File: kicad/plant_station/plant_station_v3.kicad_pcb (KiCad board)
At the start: 2 copper layers, 73.4 x 43 mm, 89 parts, among them IC1 VEML7700-TT, IC3 TLC555CDR, IC4 ADC081C021CIMK_NOPB, J1 Conn_02x08_Odd_Even, J10 I2C HOST, J11 SOIL_I2C, J12 WEATHER_I2C, J13 ZF5S-20-01-T-WT-TR, J14 505567-0471, J15 505567-0471, J16 Conn_01x06, J17 Conn_01x08, J18 Conn_01x08, J19 Ammeter_Jumper, J2 MB_I2C, J3 MB_I2C, J4 ZF5S-20-01-T-WT-TR, J5 MB_I2C, J6 MB_I2C, J7 Conn_01x08, J8 Conn_01x06, J9 I2C SCREEN, P1 USB_C_Plug_USB2.0, Q1 DTC113Z, Q3 DTC113Z, Q4 DMG2301L, Q5 BC817DS,115, U1 HDC2010YPAT, U4 ESP-WROOM-02, U5 TPL5110, U6 CP2102N-A01-GQFN28

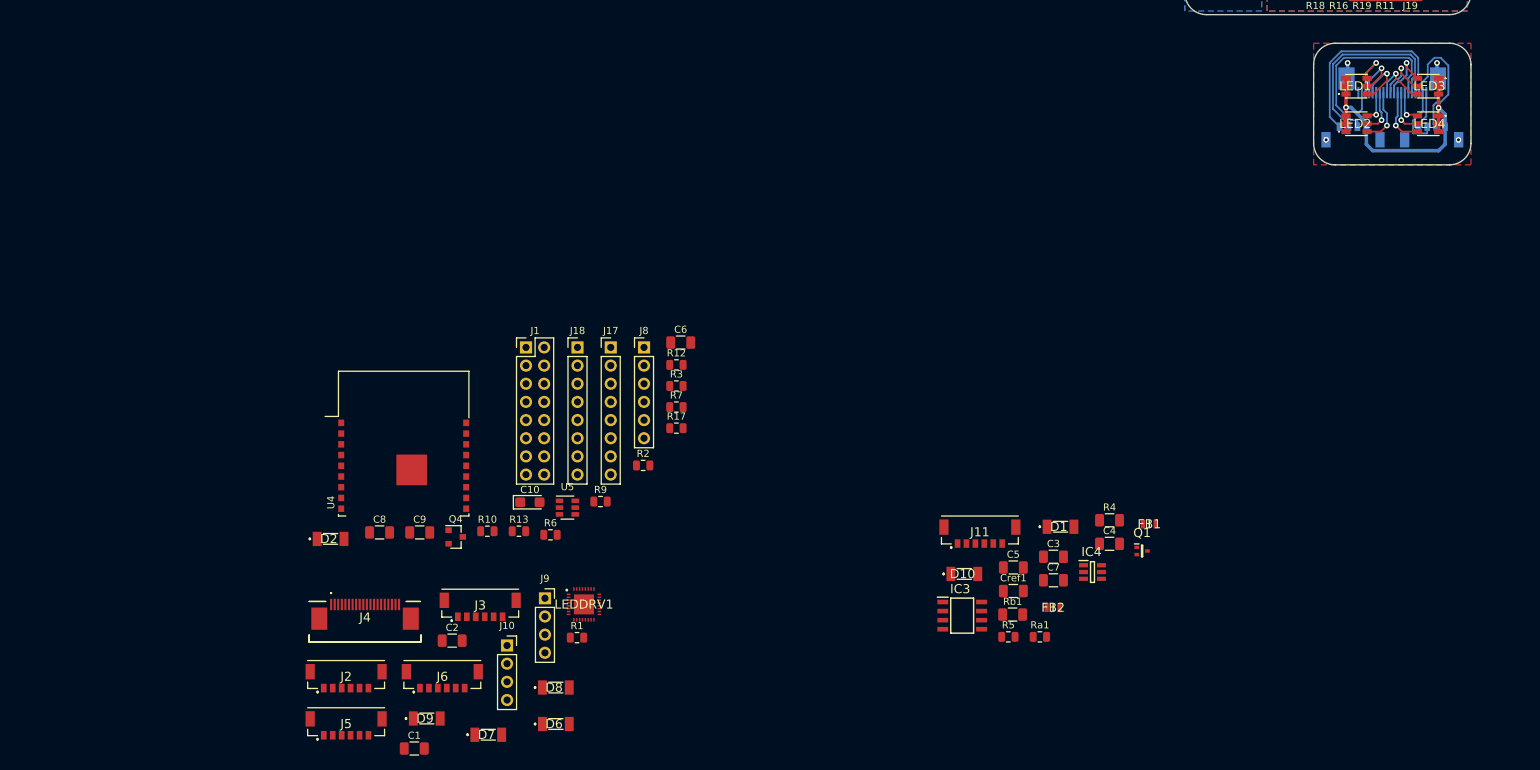
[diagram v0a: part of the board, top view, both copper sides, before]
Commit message: Moved the LED driver to LEDs board, refactored connectors. Hopefuly PCBNEW could update it all in place
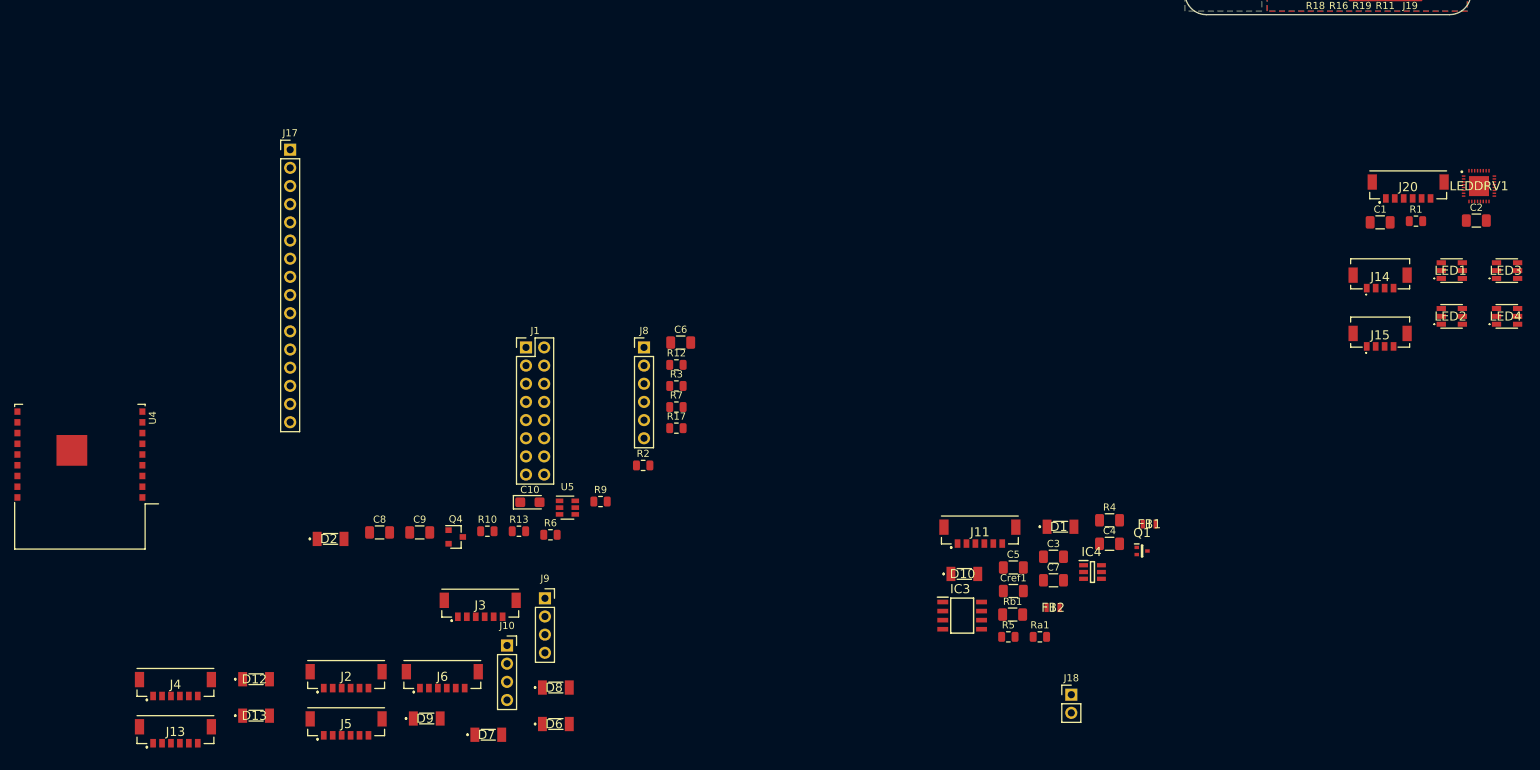
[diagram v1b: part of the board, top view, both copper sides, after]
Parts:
- added D12: LS4148, Parts:MELF_SOD_80_3_BZT55B13GS08, F.Cu at (84.1, 129.9)
- added D13: LS4148, Parts:MELF_SOD_80_3_BZT55B13GS08, F.Cu at (84.1, 135.0)
- added J20: LED_I2C, Parts:Molex_Conn_SMD_01x06_505567_0671, F.Cu at (245.2, 61.1)
- J13: value ZF5S-20-01-T-WT-TR -> MB_I2C; footprint Parts:ZF5S2001TWTTR -> Parts:Molex_Conn_SMD_01x06_505567_0671; moved to F.Cu
- J14: value 505567-0471 -> Ambient_Led_6; moved to F.Cu
- J15: value 505567-0471 -> Ambient_Led_5; moved to F.Cu
- J17: value Conn_01x08 -> GPIO; footprint Connector_PinHeader_2.54mm:PinHeader_1x08_P2.54mm_Vertical -> Connector_PinHeader_2.54mm:PinHeader_1x16_P2.54mm_Vertical
- J18: value Conn_01x08 -> ALWAYS_ON; footprint Connector_PinHeader_2.54mm:PinHeader_1x08_P2.54mm_Vertical -> Connector_PinHeader_2.54mm:PinHeader_1x02_P2.54mm_Vertical
- J4: value ZF5S-20-01-T-WT-TR -> MB_I2C; footprint Parts:ZF5S2001TWTTR -> Parts:Molex_Conn_SMD_01x06_505567_0671
- J8: value Conn_01x06 -> UART
- moved J13 193.3 mm to (72.9, 137.3)
- moved C2 154.8 mm to (254.8, 65.8)
- moved C1 153.8 mm to (241.3, 66.0)
- moved LEDDRV1 138.1 mm to (255.1, 61.0)
- moved R1 131.0 mm to (246.3, 65.9)
- moved J18 84.4 mm to (198.1, 132.1)
- moved J17 52.7 mm to (88.9, 55.9)
- moved U4 45.3 mm to (59.5, 98.5), turned to 180 degrees
- moved LED2 30.1 mm to (251.3, 79.2)
- moved LED4 29.1 mm to (259.0, 79.2), turned to 0 degrees
- moved LED1 29.0 mm to (251.3, 72.8)
- moved LED3 28.1 mm to (259.0, 72.8), turned to 0 degrees
- moved J4 27.9 mm to (72.9, 130.7)
- moved J15 27.8 mm to (241.3, 81.8)
- moved J14 20.7 mm to (241.3, 73.7)
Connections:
- net /env_sensor/HOST_WAKE renamed Net-(J12-Pad5)
- D2 pad 2: /HOST_WAKE -> /esp8266/WAKE_UP
- J1 pad 5: Net-(J1-Pad5) -> /esp8266/GPIO16
- J1 pad 6: Net-(J1-Pad6) -> /esp8266/WAKE_UP
- J1 pad 7: Net-(J1-Pad11) -> Net-(J1-Pad7)
- J13 pad 3: /leds/LED_1_R -> /SDA
- J13 pad 4: /leds/LED_1_G -> /SCL
- J13 pad 5: /leds/LED_1_B -> /HOST_WAKE
- J13 pad 6: /leds/LED_2_R -> Net-(D13-Pad1)
- J14 pad 5: Net-(J13-PadMP1) -> Net-(J14-Pad5)
- J14 pad 6: Net-(J13-PadMP1) -> Net-(J14-Pad5)
- J15 pad 5: Net-(J13-PadMP1) -> Net-(J14-Pad5)
- J15 pad 6: Net-(J13-PadMP1) -> Net-(J14-Pad5)
- J17 pad 3: /esp8266/ESP_RST -> /SDA
- J17 pad 4: /esp8266/ESP_EN -> /SCL
- J17 pad 5: /HOST_WAKE -> /esp8266/WAKE_UP
- J17 pad 6: /SDA -> /ALL_EN
- J17 pad 7: /SCL -> /esp8266/ESP_RST
- J17 pad 8: Net-(J17-Pad8) -> /esp8266/ESP_EN
- J18 pad 1: GND -> Net-(FB2-Pad1)
- J18 pad 2: +3V3 -> GND
- J2 pad MP1: Net-(J2-PadMP1) -> Net-(J13-PadMP1)
- J2 pad MP2: Net-(J2-PadMP2) -> Net-(J13-PadMP1)
- J3 pad MP1: Net-(J3-PadMP1) -> Net-(J13-PadMP1)
- J3 pad MP2: Net-(J3-PadMP2) -> Net-(J13-PadMP1)
- J4 pad 3: /LED_1_R -> /SDA
- J4 pad 4: /LED_1_G -> /SCL
- J4 pad 5: /LED_1_B -> /HOST_WAKE
- J4 pad 6: /LED_2_R -> Net-(D12-Pad1)
- J4 pad MP1: GND -> Net-(J13-PadMP1)
- J4 pad MP2: GND -> Net-(J13-PadMP1)
- J5 pad MP1: Net-(J5-PadMP1) -> Net-(J13-PadMP1)
- J5 pad MP2: Net-(J5-PadMP2) -> Net-(J13-PadMP1)
- J6 pad MP1: Net-(J6-PadMP1) -> Net-(J13-PadMP1)
- J6 pad MP2: Net-(J6-PadMP2) -> Net-(J13-PadMP1)
- LEDDRV1 pad 1: /LED_1_R -> /leds/LED_1_R
- LEDDRV1 pad 10: /LED_4_R -> /leds/LED_4_R
- LEDDRV1 pad 11: /LED_4_G -> /leds/LED_4_G
- LEDDRV1 pad 12: /LED_4_B -> /leds/LED_4_B
- LEDDRV1 pad 13: /LED_5_R -> /leds/LED_5_R
- LEDDRV1 pad 14: /LED_5_G -> /leds/LED_5_G
- LEDDRV1 pad 15: /LED_5_B -> /leds/LED_5_B
- LEDDRV1 pad 16: /LED_6_R -> /leds/LED_6_R
- LEDDRV1 pad 17: /LED_6_G -> /leds/LED_6_G
- LEDDRV1 pad 18: /LED_6_B -> /leds/LED_6_B
- LEDDRV1 pad 2: /LED_1_G -> /leds/LED_1_G
- LEDDRV1 pad 28: /SDA -> /leds/SDA
- LEDDRV1 pad 29: /SCL -> /leds/SCL
- LEDDRV1 pad 3: /LED_1_B -> /leds/LED_1_B
- LEDDRV1 pad 30: /ALL_EN -> /leds/ALL_EN
- LEDDRV1 pad 4: /LED_2_R -> /leds/LED_2_R
- LEDDRV1 pad 5: /LED_2_G -> /leds/LED_2_G
- LEDDRV1 pad 6: /LED_2_B -> /leds/LED_2_B
- LEDDRV1 pad 7: /LED_3_R -> /leds/LED_3_R
- LEDDRV1 pad 8: /LED_3_G -> /leds/LED_3_G
- LEDDRV1 pad 9: /LED_3_B -> /leds/LED_3_B
- Q4 pad 1: Net-(J1-Pad5) -> Net-(J1-Pad7)
- R7 pad 2: /HOST_WAKE -> /esp8266/WAKE_UP
- U4 pad 17: /HOST_WAKE -> /esp8266/GPIO16
- U5 pad 5: Net-(J1-Pad5) -> Net-(J1-Pad7)
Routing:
- net VDD: track 57.3 -> 15.2 mm, vias 3 -> 1
- net /leds/LED_5_B: track 28.0 -> 0.00 mm
- net /leds/LED_5_G: track 26.8 -> 0.00 mm
- net /leds/LED_5_R: track 26.7 -> 0.00 mm
- net /leds/LED_6_R: track 18.1 -> 0.00 mm
- net /leds/LED_6_G: track 9.07 -> 0.00 mm
- net /leds/LED_1_B: track 8.23 -> 0.00 mm, vias 1 -> 0
- net /leds/LED_4_R: track 8.07 -> 0.00 mm, vias 1 -> 0
- net /leds/LED_3_G: track 7.95 -> 0.00 mm, vias 1 -> 0
- net /leds/LED_2_B: track 7.92 -> 0.00 mm, vias 1 -> 0
- net /leds/LED_3_B: track 7.86 -> 0.00 mm, vias 1 -> 0
- net /leds/LED_1_G: track 7.76 -> 0.00 mm, vias 1 -> 0
- net /leds/LED_3_R: track 7.71 -> 0.00 mm, vias 1 -> 0
- net /leds/LED_1_R: track 7.46 -> 0.00 mm, vias 1 -> 0
- net /leds/LED_4_G: track 6.32 -> 0.00 mm, vias 1 -> 0
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- removed copper zone on F.Cu, net Net-(J13-PadMP1)
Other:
- board size 73.4 x 43 mm -> 73.4 x 22 mm

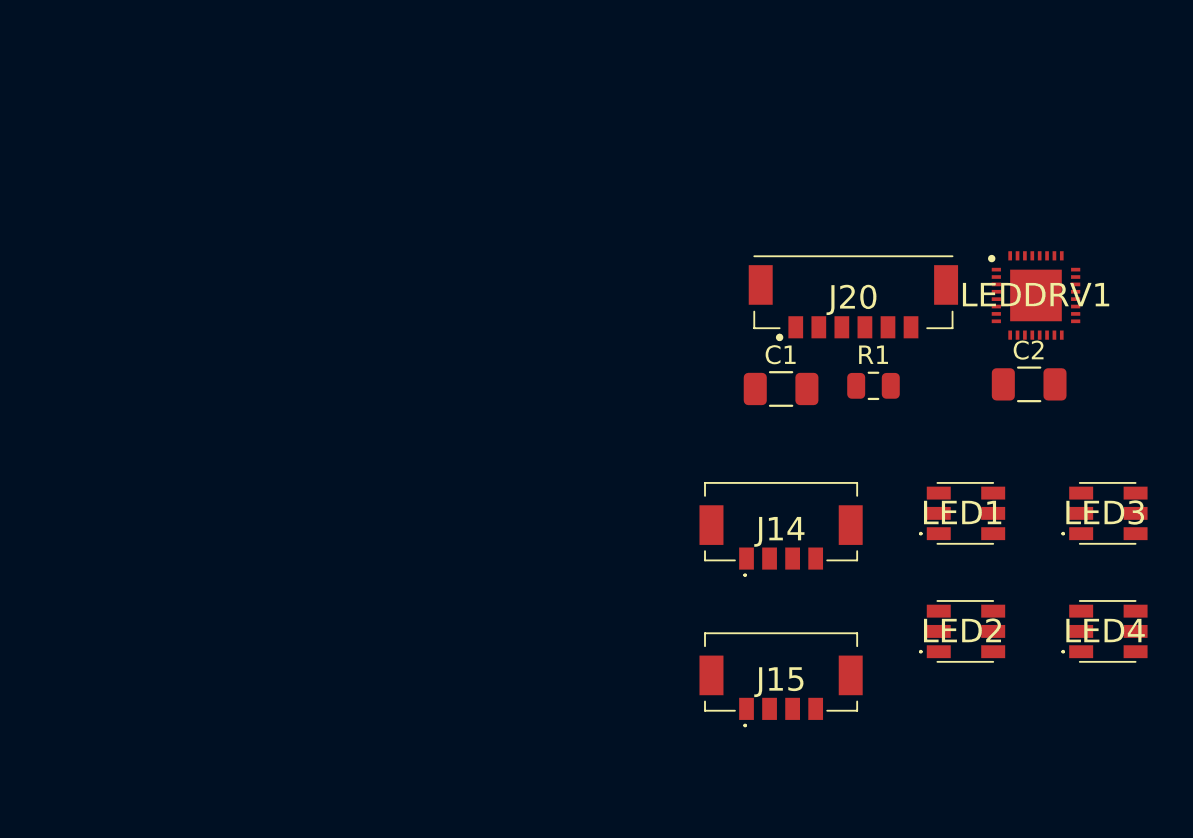
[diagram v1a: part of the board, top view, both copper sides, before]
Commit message: LEDs board done via I2C bus
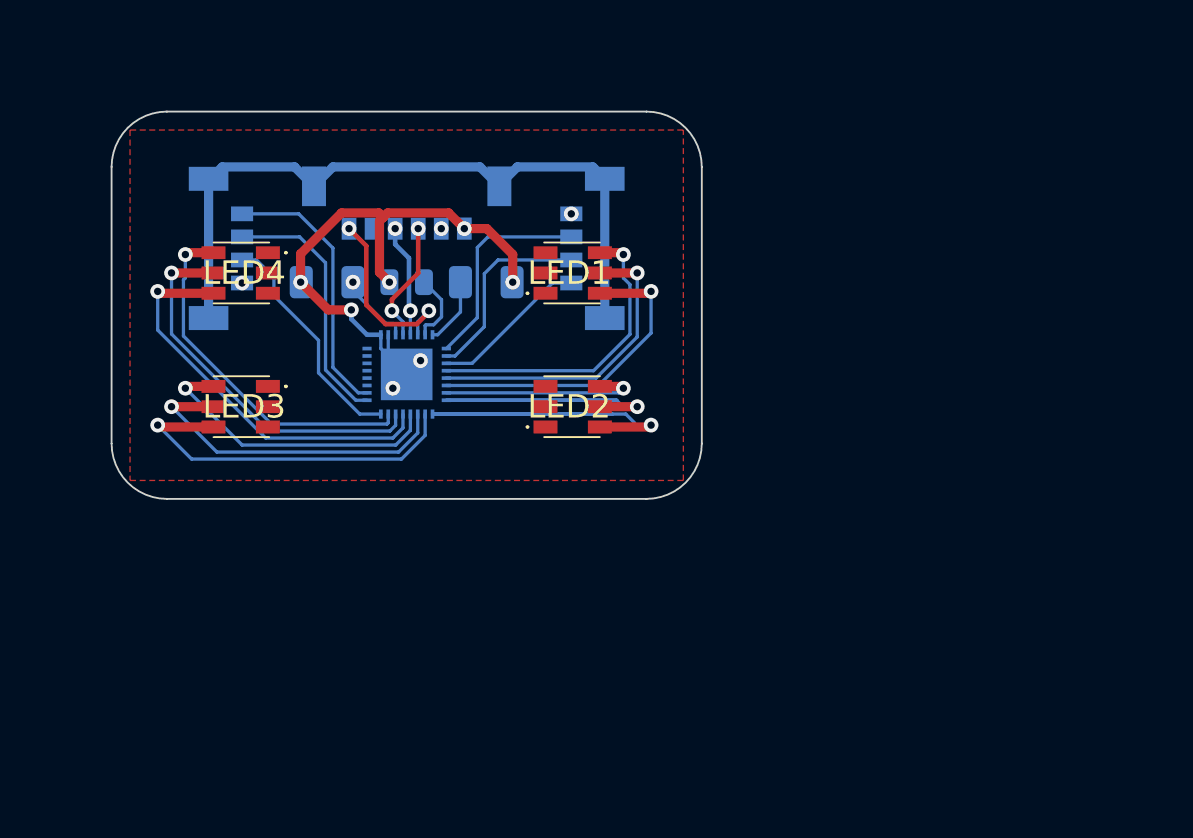
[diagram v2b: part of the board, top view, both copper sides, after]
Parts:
- C1, C2, J14, J15, J20, LEDDRV1, R1: moved to B.Cu
- moved LED4 50.9 mm to (212.0, 59.8), turned to 180 degrees
- moved LED3 47.4 mm to (212.0, 67.0), turned to 180 degrees
- moved C2 38.5 mm to (216.7, 60.2)
- moved LEDDRV1 34.4 mm to (221.0, 65.2), turned to 180 degrees
- moved J14 34.4 mm to (210.5, 58.4), turned to 270 degrees
- moved R1 25.9 mm to (221.0, 60.2)
- moved J15 25.4 mm to (231.5, 58.4), turned to 90 degrees
- moved LED1 25.0 mm to (230.0, 59.8)
- moved J20 24.8 mm to (221.0, 55.7), turned to 180 degrees
- moved LED2 24.6 mm to (230.0, 67.0)
- moved C1 17.0 mm to (225.3, 60.2)
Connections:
- J15 pad 1: /leds/LED_5_B -> /leds/LED_1_B
- J15 pad 2: /leds/LED_5_G -> /leds/LED_1_G
- J15 pad 3: /leds/LED_5_R -> /leds/LED_1_R
- LED1 pad C1: /leds/LED_1_B -> /leds/LED_2_B
- LED1 pad C2: /leds/LED_1_G -> /leds/LED_2_G
- LED1 pad C3: /leds/LED_1_R -> /leds/LED_2_R
- LED2 pad C1: /leds/LED_2_B -> /leds/LED_3_B
- LED2 pad C2: /leds/LED_2_G -> /leds/LED_3_G
- LED2 pad C3: /leds/LED_2_R -> /leds/LED_3_R
- LED3 pad C1: /leds/LED_3_B -> /leds/LED_4_B
- LED3 pad C2: /leds/LED_3_G -> /leds/LED_4_G
- LED3 pad C3: /leds/LED_3_R -> /leds/LED_4_R
- LED4 pad C1: /leds/LED_4_B -> /leds/LED_5_B
- LED4 pad C2: /leds/LED_4_G -> /leds/LED_5_G
- LED4 pad C3: /leds/LED_4_R -> /leds/LED_5_R
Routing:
- net Net-(J14-Pad5): track 0.00 -> 39.1 mm
- net GND: track 36.6 -> 68.1 mm, vias 8 -> 15
- net /leds/LED_3_B: track 0.00 -> 24.7 mm, vias 0 -> 1
- net /leds/LED_5_R: track 0.00 -> 21.9 mm, vias 0 -> 1
- net /leds/LED_3_G: track 0.00 -> 21.8 mm, vias 0 -> 1
- net /leds/LED_5_G: track 0.00 -> 20.7 mm, vias 0 -> 1
- net /leds/LED_4_R: track 0.00 -> 20.0 mm, vias 0 -> 1
- net /leds/LED_5_B: track 0.00 -> 19.6 mm, vias 0 -> 1
- net /leds/LED_4_G: track 0.00 -> 18.1 mm, vias 0 -> 1
- net /leds/LED_2_B: track 0.00 -> 17.4 mm, vias 0 -> 1
- net /leds/LED_2_G: track 0.00 -> 16.8 mm, vias 0 -> 1
- net /leds/LED_2_R: track 0.00 -> 16.6 mm, vias 0 -> 1
- net /leds/LED_4_B: track 0.00 -> 16.3 mm, vias 0 -> 1
- net /leds/LED_6_B: track 0.00 -> 14.6 mm
- net /leds/LED_6_G: track 0.00 -> 13.8 mm
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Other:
- board size 73.4 x 22 mm -> 73.4 x 57 mm

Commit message: Initial board layout complete
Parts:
- removed D7: LS4148, Parts:MELF_SOD_80_3_BZT55B13GS08
- removed J3: MB_I2C, Parts:Molex_Conn_SMD_01x06_505567_0671
- added REF**: MountingHole_2.2mm_M2_ISO7380, MountingHole:MountingHole_2.2mm_M2_ISO7380, F.Cu at (220.9, 46.5)
- added REF**: MountingHole_2.2mm_M2_ISO7380, MountingHole:MountingHole_2.2mm_M2_ISO7380, F.Cu at (207.2, 62.7)
- added REF**: MountingHole_2.2mm_M2_ISO7380, MountingHole:MountingHole_2.2mm_M2_ISO7380, F.Cu at (186.0, 61.0)
- added REF**: MountingHole_2.2mm_M2_ISO7380, MountingHole:MountingHole_2.2mm_M2_ISO7380, F.Cu at (185.9, 43.4)
- added REF**: MountingHole_2.2mm_M2_ISO7380, MountingHole:MountingHole_2.2mm_M2_ISO7380, F.Cu at (185.9, 25.9)
- D12, D13, D6, D8, D9, J11, J13, J17, J2, J4, J5, J6: moved to B.Cu
- moved U4 157.9 mm to (203.7, 34.3), turned to 310.5 degrees
- moved J4 155.7 mm to (208.0, 53.2), turned to 90 degrees
- moved J13 148.7 mm to (195.5, 53.2), turned to 270 degrees
- moved C13 147.2 mm to (326.8, -18.8)
- moved C14 147.2 mm to (331.5, -18.8)
- moved IC1 147.2 mm to (335.0, -16.0)
- moved J12 147.2 mm to (329.0, -14.3)
- moved Q3 147.2 mm to (329.0, -10.8)
- moved U1 147.2 mm to (325.5, -14.8)
- moved D12 144.0 mm to (203.8, 49.8), turned to 90 degrees
- moved J2 142.4 mm to (206.2, 38.5), turned to 90 degrees
- moved D9 139.7 mm to (196.2, 27.1), turned to 270 degrees
- moved D13 139.7 mm to (199.8, 56.6), turned to 270 degrees
- moved J5 137.7 mm to (193.8, 38.5), turned to 270 degrees
- moved J6 133.8 mm to (192.0, 23.8), turned to 270 degrees
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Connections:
- J1 pad 1: VDD -> /esp8266/WAKE_UP
- J1 pad 10: Net-(J1-Pad10) -> +3V3
- J1 pad 2: +3V3 -> /esp8266/GPIO16
- J1 pad 4: Net-(J1-Pad10) -> +3V3
- J1 pad 5: /esp8266/GPIO16 -> VDD
- J1 pad 6: /esp8266/WAKE_UP -> Net-(J1-Pad12)
- J1 pad 8: +3V3 -> Net-(J1-Pad8)
- J1 pad 9: Net-(J1-Pad11) -> Net-(J1-Pad7)
- J13 pad MP2: Net-(J13-PadMP1) -> Net-(J13-PadMP2)
- J17 pad 12: /esp8266/GPIO12 -> /esp8266/GPIO15
- J17 pad 14: /esp8266/GPIO15 -> /esp8266/GPIO12
- J17 pad 5: /esp8266/WAKE_UP -> +3V3
- J17 pad 9: +3V3 -> /esp8266/WAKE_UP
- J2 pad MP1: Net-(J13-PadMP1) -> Net-(J2-PadMP1)
- J2 pad MP2: Net-(J13-PadMP1) -> Net-(J2-PadMP2)
- J4 pad MP1: Net-(J13-PadMP1) -> Net-(J4-PadMP1)
- J4 pad MP2: Net-(J13-PadMP1) -> Net-(J4-PadMP2)
- J5 pad MP1: Net-(J13-PadMP1) -> Net-(J5-PadMP1)
- J5 pad MP2: Net-(J13-PadMP1) -> Net-(J5-PadMP2)
- J6 pad MP1: Net-(J13-PadMP1) -> Net-(J6-PadMP1)
- J6 pad MP2: Net-(J13-PadMP1) -> Net-(J6-PadMP2)
- Q4 pad 1: Net-(J1-Pad7) -> Net-(J1-Pad11)
- Q4 pad 3: Net-(J1-Pad11) -> Net-(J1-Pad7)
- R17 pad 2: Net-(J1-Pad10) -> Net-(J1-Pad12)
- U5 pad 5: Net-(J1-Pad7) -> Net-(J1-Pad11)
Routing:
- net GND: track 68.1 -> 320.4 mm, vias 15 -> 24
- net VDD: track 19.3 -> 243.9 mm, vias 5 -> 13
- net /SCL: track 0.00 -> 172.9 mm, vias 0 -> 2
- net /SDA: track 0.00 -> 161.1 mm, vias 0 -> 2
- net /ALL_EN: track 0.00 -> 147.2 mm, vias 0 -> 1
- net /HOST_WAKE: track 0.00 -> 130.7 mm
- net +3V3: track 0.00 -> 89.1 mm, vias 0 -> 3
- net /esp8266/WAKE_UP: track 0.00 -> 81.6 mm, vias 0 -> 1
- net /esp8266/ESP_EN: track 0.00 -> 79.5 mm, vias 0 -> 2
- net /esp8266/GPIO5: track 0.00 -> 61.5 mm, vias 0 -> 2
- net /esp8266/ESP_RST: track 0.00 -> 57.7 mm, vias 0 -> 1
- net /esp8266/USB_RXD: track 0.00 -> 47.3 mm, vias 0 -> 1
- net /esp8266/GPIO16: track 0.00 -> 47.3 mm
- net /esp8266/USB_TXD: track 0.00 -> 45.4 mm, vias 0 -> 1
- net /esp8266/GPIO15: track 0.00 -> 37.5 mm
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- added copper zone on B.Cu, net (none)
- added copper zone on F.Cu, net (none)
- added copper zone on F.Cu, net /moisture_sensor/GNDA
- added copper zone on B.Cu, net /moisture_sensor/VA
- added copper zone on B.Cu, net VDD
- removed copper zone on B.Cu, net /env_sensor/GNDA
- removed copper zone on B.Cu, net Net-(P1-PadS1)
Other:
- board size 73.4 x 57 mm -> 160.8 x 185 mm
